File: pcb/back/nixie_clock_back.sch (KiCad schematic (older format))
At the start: 16 parts, among them J1 Conn_01x10_Male, J2 Conn_01x10_Male, J3 ICSP, J4 5V_IN, J5 HV_IN, SW1 BTN2, SW2 BTN1, U1 ATmega328P-PU, U2 DS1307, Y1 32768Hz

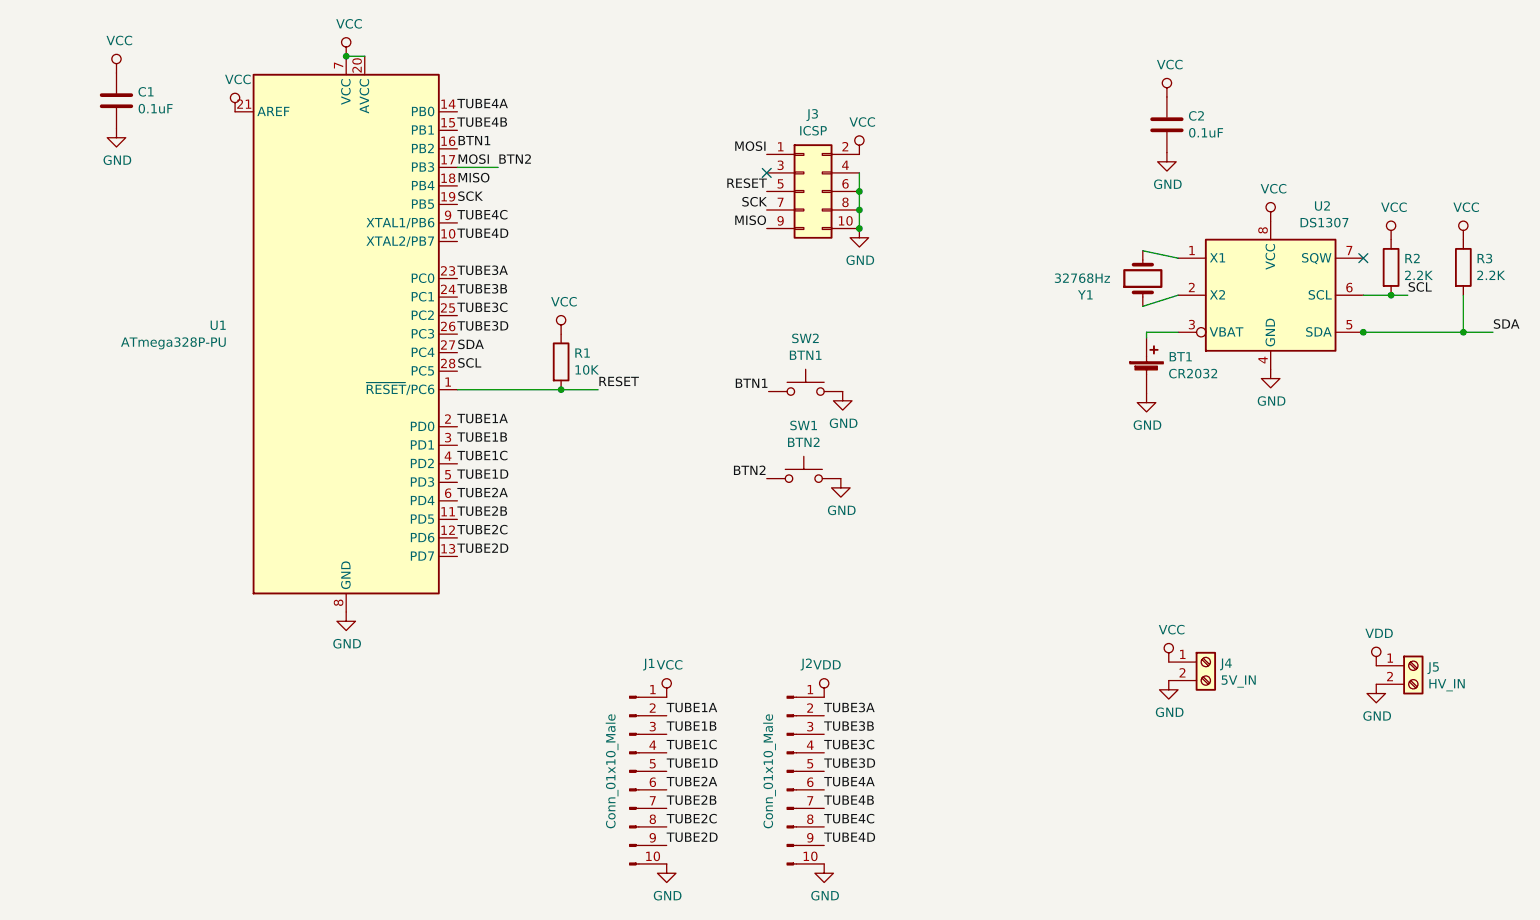
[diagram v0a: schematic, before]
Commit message: Back panel PCB
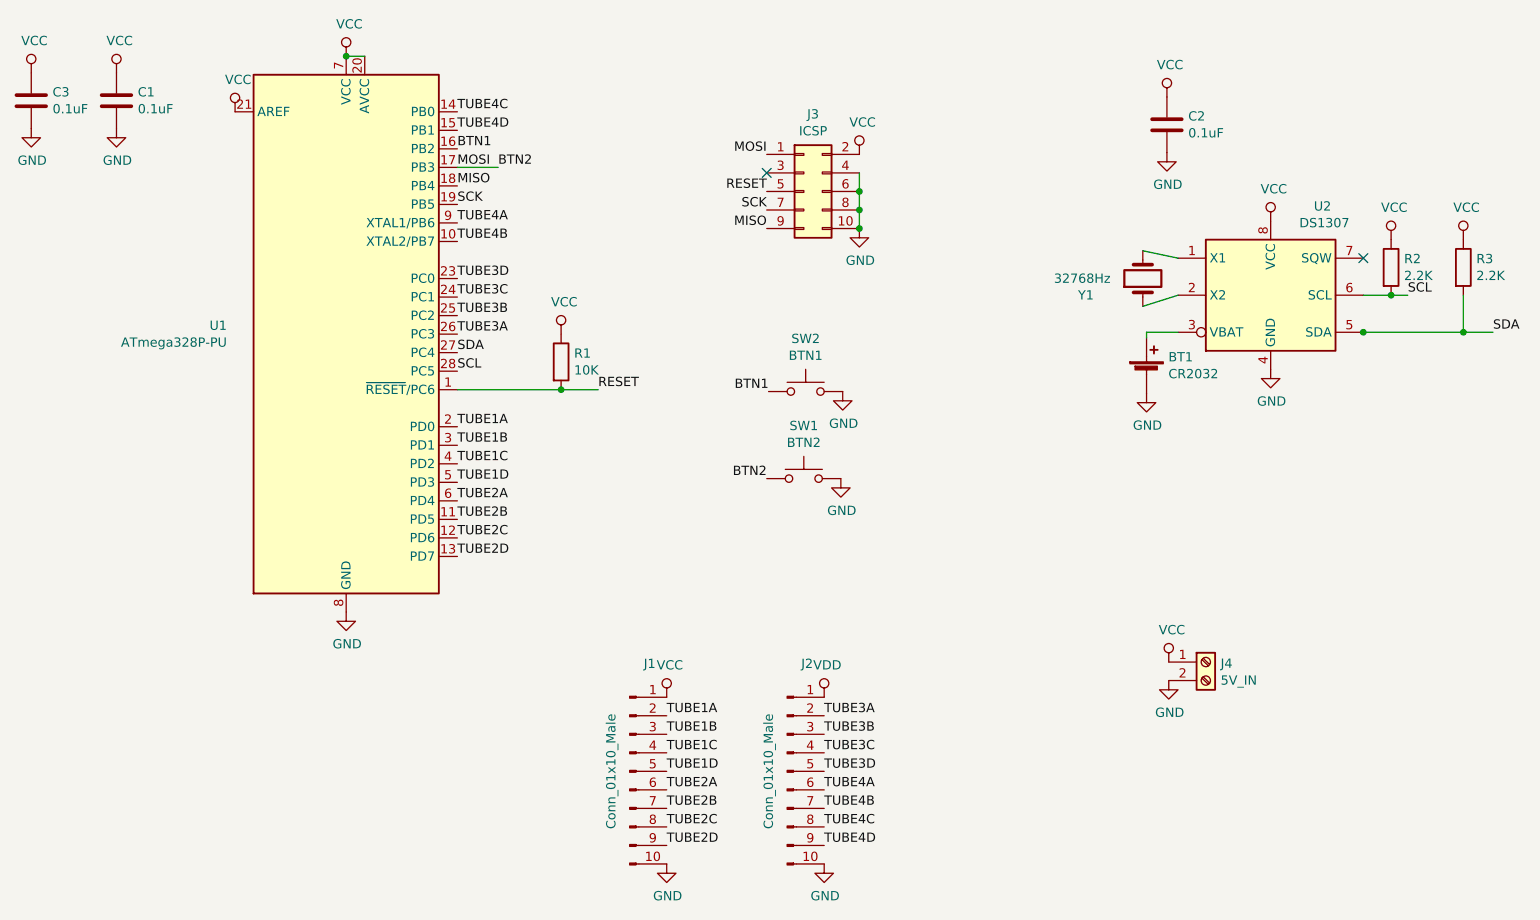
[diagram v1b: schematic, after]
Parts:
- removed J5: HV_IN, symbol Connector:Screw_Terminal_01x02
- added C3: 0.1uF, Capacitor_THT:C_Disc_D3.8mm_W2.6mm_P2.50mm, symbol Device:C
- BT1: footprint (none) -> Battery:BatteryHolder_Keystone_103_1x20mm
- J1, J2: footprint (none) -> Connector_PinSocket_2.54mm:PinSocket_1x10_P2.54mm_Vertical
- J3: footprint (none) -> nixie_clock:Atmel_ISP_Socket_10pin
- J4: footprint (none) -> nixie_clock:Terminal_Block_KF301-5.0-2P
- SW1, SW2: footprint (none) -> Connector_JST:JST_XH_B2B-XH-A_1x02_P2.50mm_Vertical
- Y1: footprint (none) -> Crystal:Crystal_C38-LF_D3.0mm_L8.0mm_Horizontal
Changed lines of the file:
@@
 F 0 "J1" H 4318 5751 50  0000 C CNN
 F 1 "Conn_01x10_Male" V 4110 5170 50  0000 C CNN
-F 2 "" H 4210 5170 50  0001 C CNN
+F 2 "Connector_PinSocket_2.54mm:PinSocket_1x10_P2.54mm_Vertical" H 4210 5170 50  0001 C CNN
 F 3 "~" H 4210 5170 50  0001 C CNN
 	1    4210 5170
@@
 F 0 "J2" H 5168 5751 50  0000 C CNN
 F 1 "Conn_01x10_Male" V 4960 5170 50  0000 C CNN
-F 2 "" H 5060 5170 50  0001 C CNN
+F 2 "Connector_PinSocket_2.54mm:PinSocket_1x10_P2.54mm_Vertical" H 5060 5170 50  0001 C CNN
 F 3 "~" H 5060 5170 50  0001 C CNN
 	1    5060 5170
@@
 F 0 "Y1" V 6890 2860 50  0000 R CNN
 F 1 "32768Hz" V 6980 2990 50  0000 R CNN
-F 2 "" H 6980 2510 50  0001 C CNN
+F 2 "Crystal:Crystal_C38-LF_D3.0mm_L8.0mm_Horizontal" H 6980 2510 50  0001 C CNN
 F 3 "~" H 6980 2510 50  0001 C CNN
 	1    6980 2510
@@
 F 0 "BT1" H 7118 3126 50  0000 L CNN
 F 1 "CR2032" H 7118 3035 50  0000 L CNN
-F 2 "" V 7000 3090 50  0001 C CNN
+F 2 "Battery:BatteryHolder_Keystone_103_1x20mm" V 7000 3090 50  0001 C CNN
 F 3 "~" V 7000 3090 50  0001 C CNN
 	1    7000 3030
@@
 F 0 "J4" H 7400 4572 50  0000 L CNN
 F 1 "5V_IN" H 7400 4481 50  0000 L CNN
-F 2 "" H 7320 4580 50  0001 C CNN
+F 2 "nixie_clock:Terminal_Block_KF301-5.0-2P" H 7320 4580 50  0001 C CNN
 F 3 "~" H 7320 4580 50  0001 C CNN
 	1    7320 4580
@@
 $EndComp
 $Comp
-L Connector:Screw_Terminal_01x02 J5
-U 1 1 5DB1F008
-P 8440 4600
-F 0 "J5" H 8520 4592 50  0000 L CNN
-F 1 "HV_IN" H 8520 4501 50  0000 L CNN
-F 2 "" H 8440 4600 50  0001 C CNN
-F 3 "~" H 8440 4600 50  0001 C CNN
-	1    8440 4600
-	1    0    0    -1
-$EndComp
-$Comp
-L power:VDD #PWR0114
-U 1 1 5DB1FA41
-P 8240 4600
-F 0 "#PWR0114" H 8240 4450 50  0001 C CNN
-F 1 "VDD" H 8257 4773 50  0000 C CNN
-F 2 "" H 8240 4600 50  0001 C CNN
-F 3 "" H 8240 4600 50  0001 C CNN
-	1    8240 4600
-	1    0    0    -1
-$EndComp
-$Comp
-L power:GND #PWR0115
-U 1 1 5DB204E0
-P 8240 4700
-F 0 "#PWR0115" H 8240 4450 50  0001 C CNN
-F 1 "GND" H 8245 4527 50  0000 C CNN
-F 2 "" H 8240 4700 50  0001 C CNN
-F 3 "" H 8240 4700 50  0001 C CNN
-	1    8240 4700
-	1    0    0    -1
-$EndComp
-$Comp
 L Switch:SW_Push SW2
 U 1 1 5DB22E25
@@
 F 0 "SW2" H 5160 3405 50  0000 C CNN
 F 1 "BTN1" H 5160 3314 50  0000 C CNN
-F 2 "" H 5160 3320 50  0001 C CNN
+F 2 "Connector_JST:JST_XH_B2B-XH-A_1x02_P2.50mm_Vertical" H 5160 3320 50  0001 C CNN
 F 3 "~" H 5160 3320 50  0001 C CNN
 	1    5160 3120
@@
 F 0 "SW1" H 5150 3875 50  0000 C CNN
 F 1 "BTN2" H 5150 3784 50  0000 C CNN
-F 2 "" H 5150 3790 50  0001 C CNN
+F 2 "Connector_JST:JST_XH_B2B-XH-A_1x02_P2.50mm_Vertical" H 5150 3790 50  0001 C CNN
 F 3 "~" H 5150 3790 50  0001 C CNN
 	1    5150 3590
@@
 F 0 "J3" H 5200 2457 50  0000 C CNN
 F 1 "ICSP" H 5200 2366 50  0000 C CNN
-F 2 "" H 5150 2040 50  0001 C CNN
+F 2 "nixie_clock:Atmel_ISP_Socket_10pin" H 5150 2040 50  0001 C CNN
 F 3 "~" H 5150 2040 50  0001 C CNN
 	1    5150 2040
@@
 Text Label 3280 4010 0    50   ~ 0
 TUBE2D
+Text Label 3280 2810 0    50   ~ 0
+TUBE3A
+Text Label 3280 2710 0    50   ~ 0
+TUBE3B
+Text Label 3280 2610 0    50   ~ 0
+TUBE3C
 Text Label 3280 2510 0    50   ~ 0
-TUBE3A
-Text Label 3280 2610 0    50   ~ 0
-TUBE3B
-Text Label 3280 2710 0    50   ~ 0
-TUBE3C
-Text Label 3280 2810 0    50   ~ 0
 TUBE3D
+Text Label 3280 2210 0    50   ~ 0
+TUBE4A
+Text Label 3280 2310 0    50   ~ 0
+TUBE4B
 Text Label 3280 1610 0    50   ~ 0
-TUBE4A
-Text Label 3280 1710 0    50   ~ 0
-TUBE4B
-Text Label 3280 2210 0    50   ~ 0
 TUBE4C
 Text Label 3280 1810 0    50   ~ 0
@@
 Text Label 3500 1910 0    50   ~ 0
 BTN2
-Text Label 3280 2310 0    50   ~ 0
+Text Label 3280 1710 0    50   ~ 0
 TUBE4D
 $Comp
@@
 	1    0    0    -1
 $EndComp
+$Comp
+L Device:C C3
+U 1 1 5DAD93AA
+P 980 1550
+F 0 "C3" H 1095 1596 50  0000 L CNN
+F 1 "0.1uF" H 1095 1505 50  0000 L CNN
+F 2 "Capacitor_THT:C_Disc_D3.8mm_W2.6mm_P2.50mm" H 1018 1400 50  0001 C CNN
+F 3 "~" H 980 1550 50  0001 C CNN
+	1    980  1550
+	1    0    0    -1
+$EndComp
+$Comp
+L power:VCC #PWR05
+U 1 1 5DAD93B4
+P 980 1400
+F 0 "#PWR05" H 980 1250 50  0001 C CNN
+F 1 "VCC" H 997 1573 50  0000 C CNN
+F 2 "" H 980 1400 50  0001 C CNN
+F 3 "" H 980 1400 50  0001 C CNN
+	1    980  1400
+	1    0    0    -1
+$EndComp
+$Comp
+L power:GND #PWR06
+U 1 1 5DAD93BE
+P 980 1700
+F 0 "#PWR06" H 980 1450 50  0001 C CNN
+F 1 "GND" H 985 1527 50  0000 C CNN
+F 2 "" H 980 1700 50  0001 C CNN
+F 3 "" H 980 1700 50  0001 C CNN
+	1    980  1700
+	1    0    0    -1
+$EndComp
